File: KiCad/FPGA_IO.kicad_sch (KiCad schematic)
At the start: 18 parts, among them U502 XC7S50FTGB196

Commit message: replaced SAR-ADC with Sigma-Delta-Converter
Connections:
- net ADC.COMP: no longer names the net of U502.B6 (IO_0_34)
- net ADC.D0: no longer names the net of U502.D1 (IO_L11P_T1_SRCC_34)
- net ADC.D1: no longer names the net of U502.D2 (IO_L10N_T1_34)
- net ADC.D2: no longer names the net of U502.B1 (IO_L5N_T0_34)
- net ADC.D3 renamed ADC.FB_out0
- net ADC.D4: no longer names the net of U502.B2 (IO_L5P_T0_34)
- net ADC.D5 renamed ADC.SD_in0
- net ADC.D6: no longer names the net of U502.B3 (IO_L3P_T0_DQS_34)
- net ADC.D7 renamed ADC.SD_in1
- net ADC.SEL: no longer names the net of U502.B5 (IO_L4P_T0_34)
- net ADC.SH renamed ADC.FB_out1

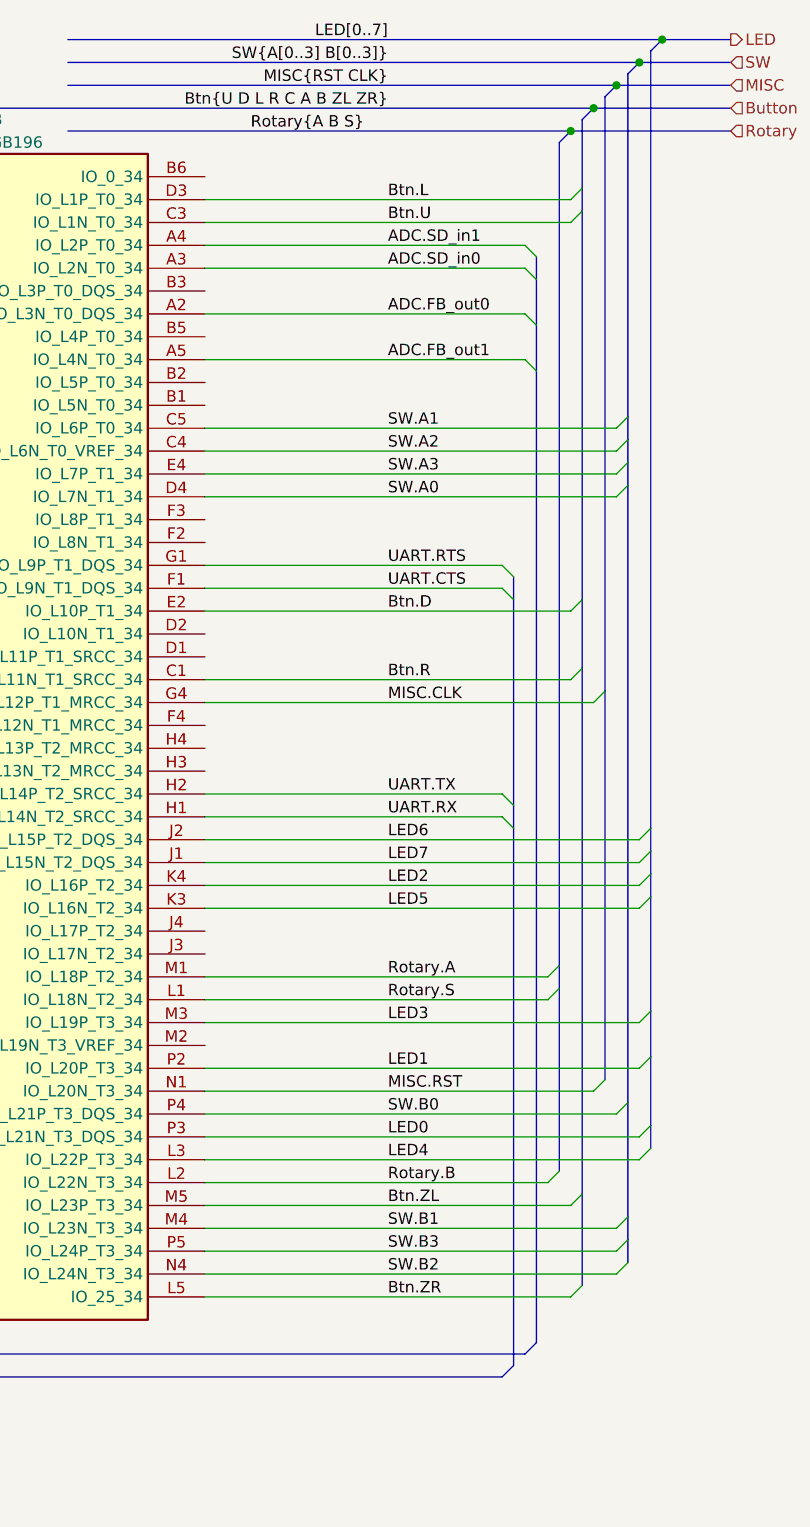
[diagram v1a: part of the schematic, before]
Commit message: Vorberitung für micro-SD
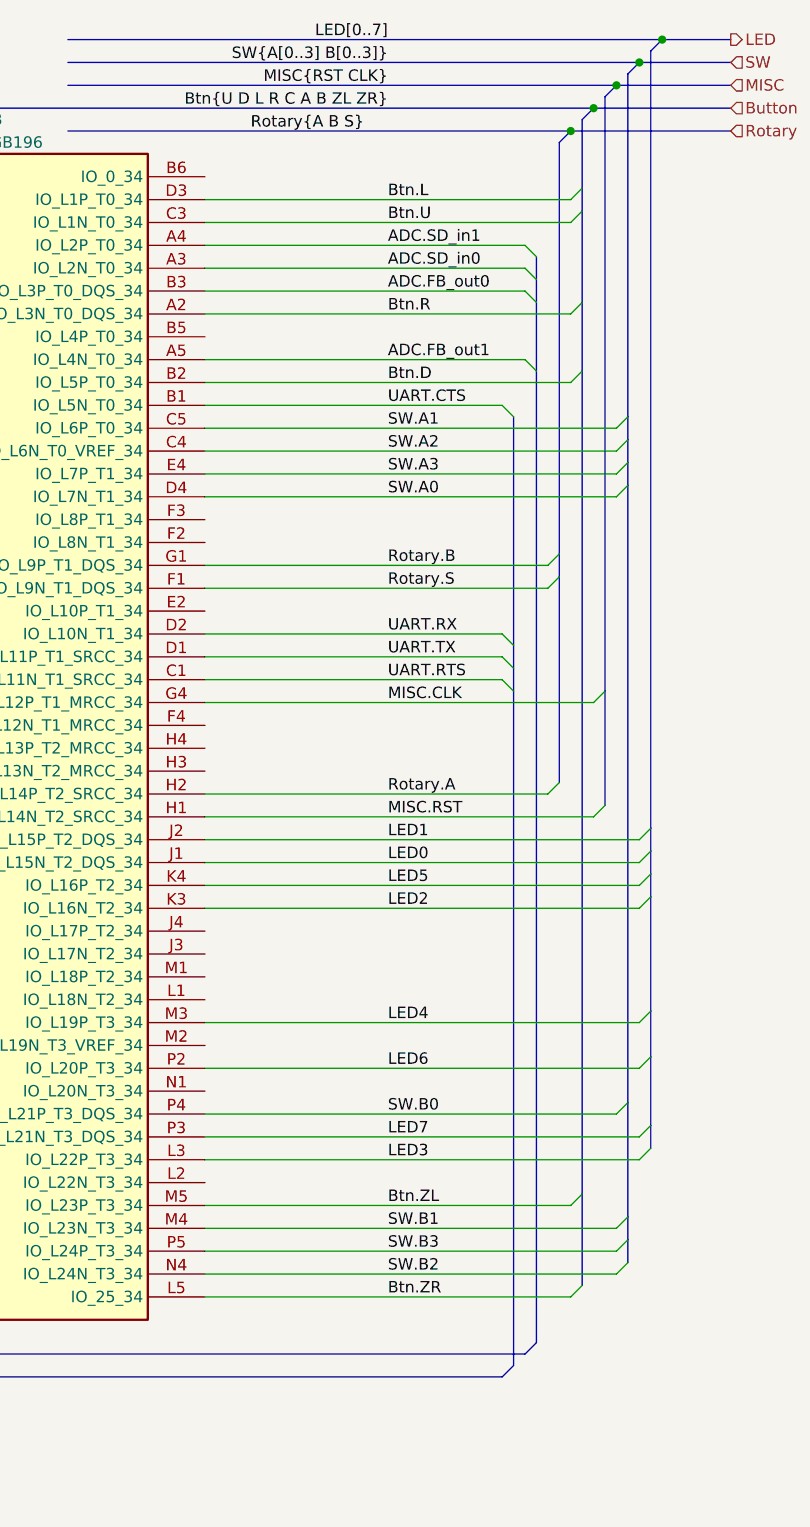
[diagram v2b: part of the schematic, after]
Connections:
- net ADC.FB_out0: now also U502.B3 (IO_L3P_T0_DQS_34); no longer U502.A2 (IO_L3N_T0_DQS_34)
- net Btn.D: now also U502.B2 (IO_L5P_T0_34); no longer U502.E2 (IO_L10P_T1_34)
- net Btn.R: now also U502.A2 (IO_L3N_T0_DQS_34); no longer U502.C1 (IO_L11N_T1_SRCC_34)
- net LED0: now also U502.J1 (IO_L15N_T2_DQS_34); no longer U502.P3 (IO_L21N_T3_DQS_34)
- net LED1: now also U502.J2 (IO_L15P_T2_DQS_34); no longer U502.P2 (IO_L20P_T3_34)
- net LED2: now also U502.K3 (IO_L16N_T2_34); no longer U502.K4 (IO_L16P_T2_34)
- net LED3: now also U502.L3 (IO_L22P_T3_34); no longer U502.M3 (IO_L19P_T3_34)
- net LED4: now also U502.M3 (IO_L19P_T3_34); no longer U502.L3 (IO_L22P_T3_34)
- net LED5: now also U502.K4 (IO_L16P_T2_34); no longer U502.K3 (IO_L16N_T2_34)
- net LED6: now also U502.P2 (IO_L20P_T3_34); no longer U502.J2 (IO_L15P_T2_DQS_34)
- net LED7: now also U502.P3 (IO_L21N_T3_DQS_34); no longer U502.J1 (IO_L15N_T2_DQS_34)
- net MISC.RST: now also U502.H1 (IO_L14N_T2_SRCC_34); no longer U502.N1 (IO_L20N_T3_34)
- net Rotary.A: now also U502.H2 (IO_L14P_T2_SRCC_34); no longer U502.M1 (IO_L18P_T2_34)
- net Rotary.B: now also U502.G1 (IO_L9P_T1_DQS_34); no longer U502.L2 (IO_L22N_T3_34)
- net Rotary.S: now also U502.F1 (IO_L9N_T1_DQS_34); no longer U502.L1 (IO_L18N_T2_34)
- net UART.CTS: now also U502.B1 (IO_L5N_T0_34); no longer U502.F1 (IO_L9N_T1_DQS_34)
- net UART.RTS: now also U502.C1 (IO_L11N_T1_SRCC_34); no longer U502.G1 (IO_L9P_T1_DQS_34)
- net UART.RX: now also U502.D2 (IO_L10N_T1_34); no longer U502.H1 (IO_L14N_T2_SRCC_34)
- net UART.TX: now also U502.D1 (IO_L11P_T1_SRCC_34); no longer U502.H2 (IO_L14P_T2_SRCC_34)

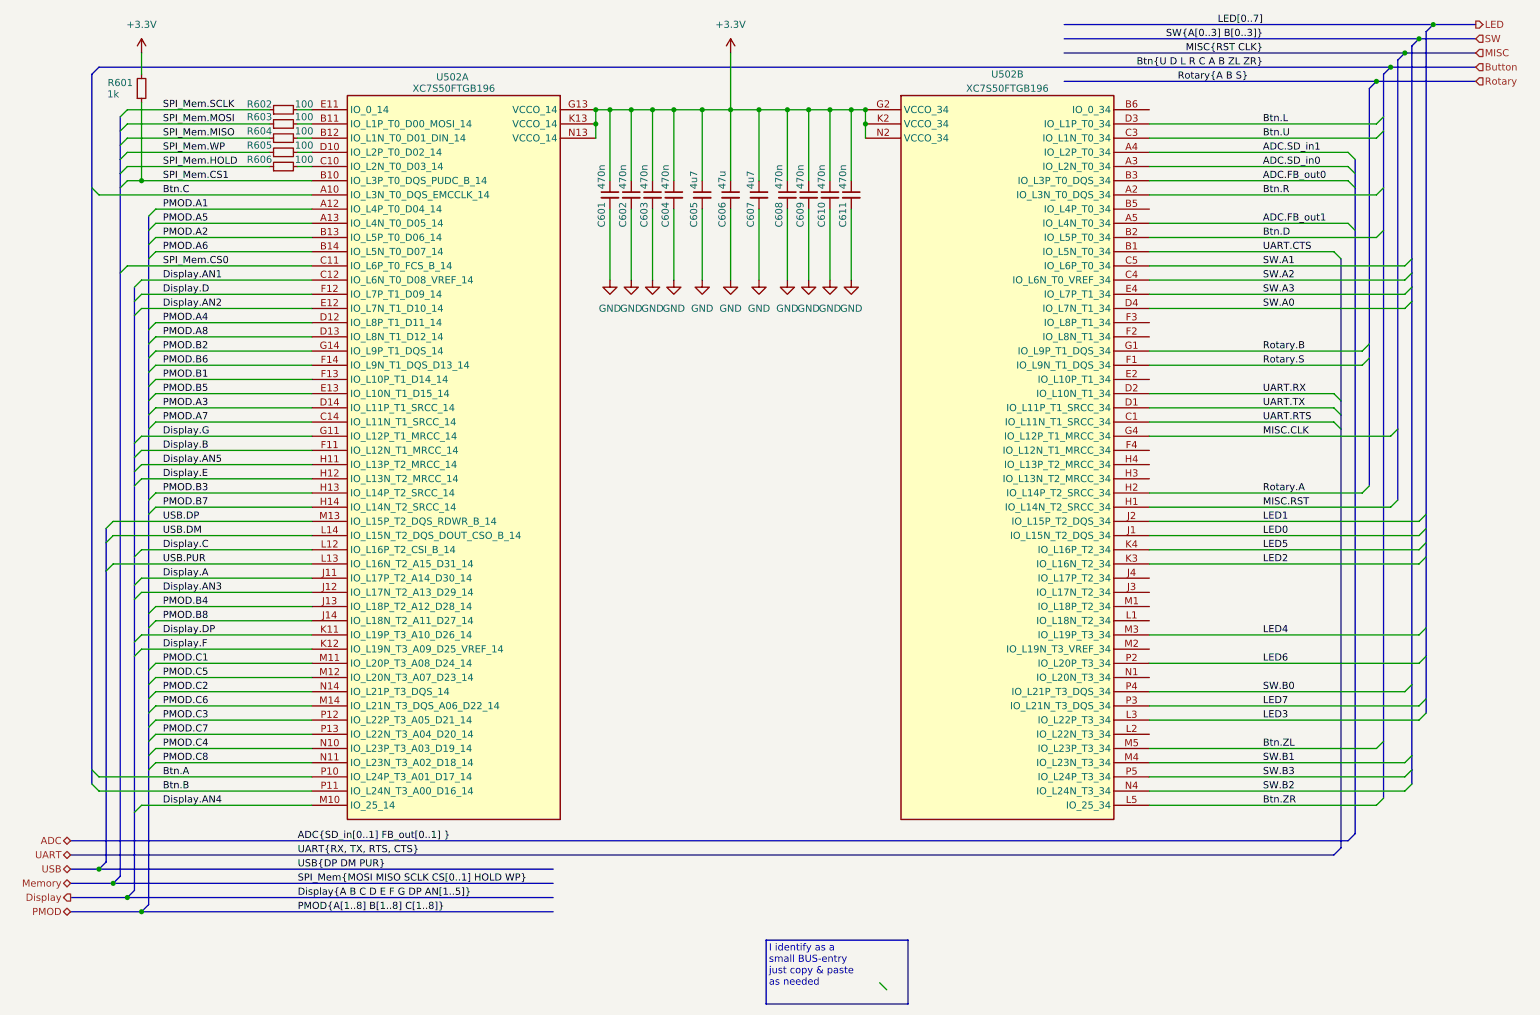
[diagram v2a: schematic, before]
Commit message: micro-SD hinzugefügt
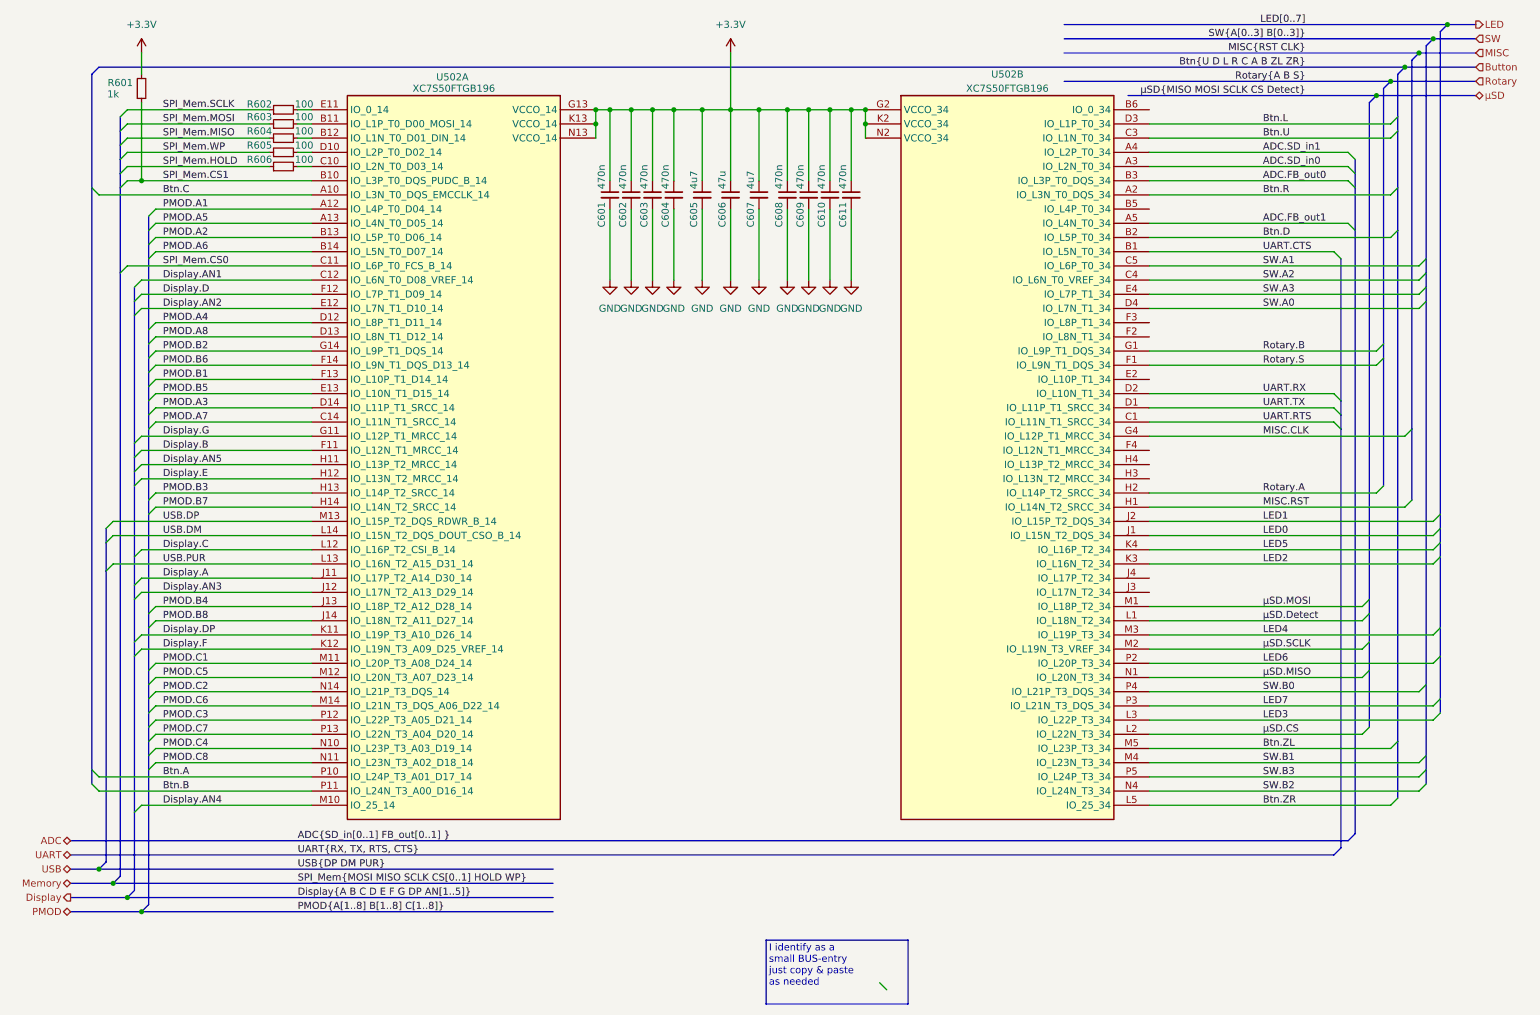
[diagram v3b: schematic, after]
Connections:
- net μSD.Detect: now reaches U502.L1 (IO_L18N_T2_34)
- net μSD.CS: now reaches U502.L2 (IO_L22N_T3_34)
- net μSD.MOSI: now reaches U502.M1 (IO_L18P_T2_34)
- net μSD.SCLK: now reaches U502.M2 (IO_L19N_T3_VREF_34)
- net μSD.MISO: now reaches U502.N1 (IO_L20N_T3_34)

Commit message: Pinout und Silkscreen angepasst
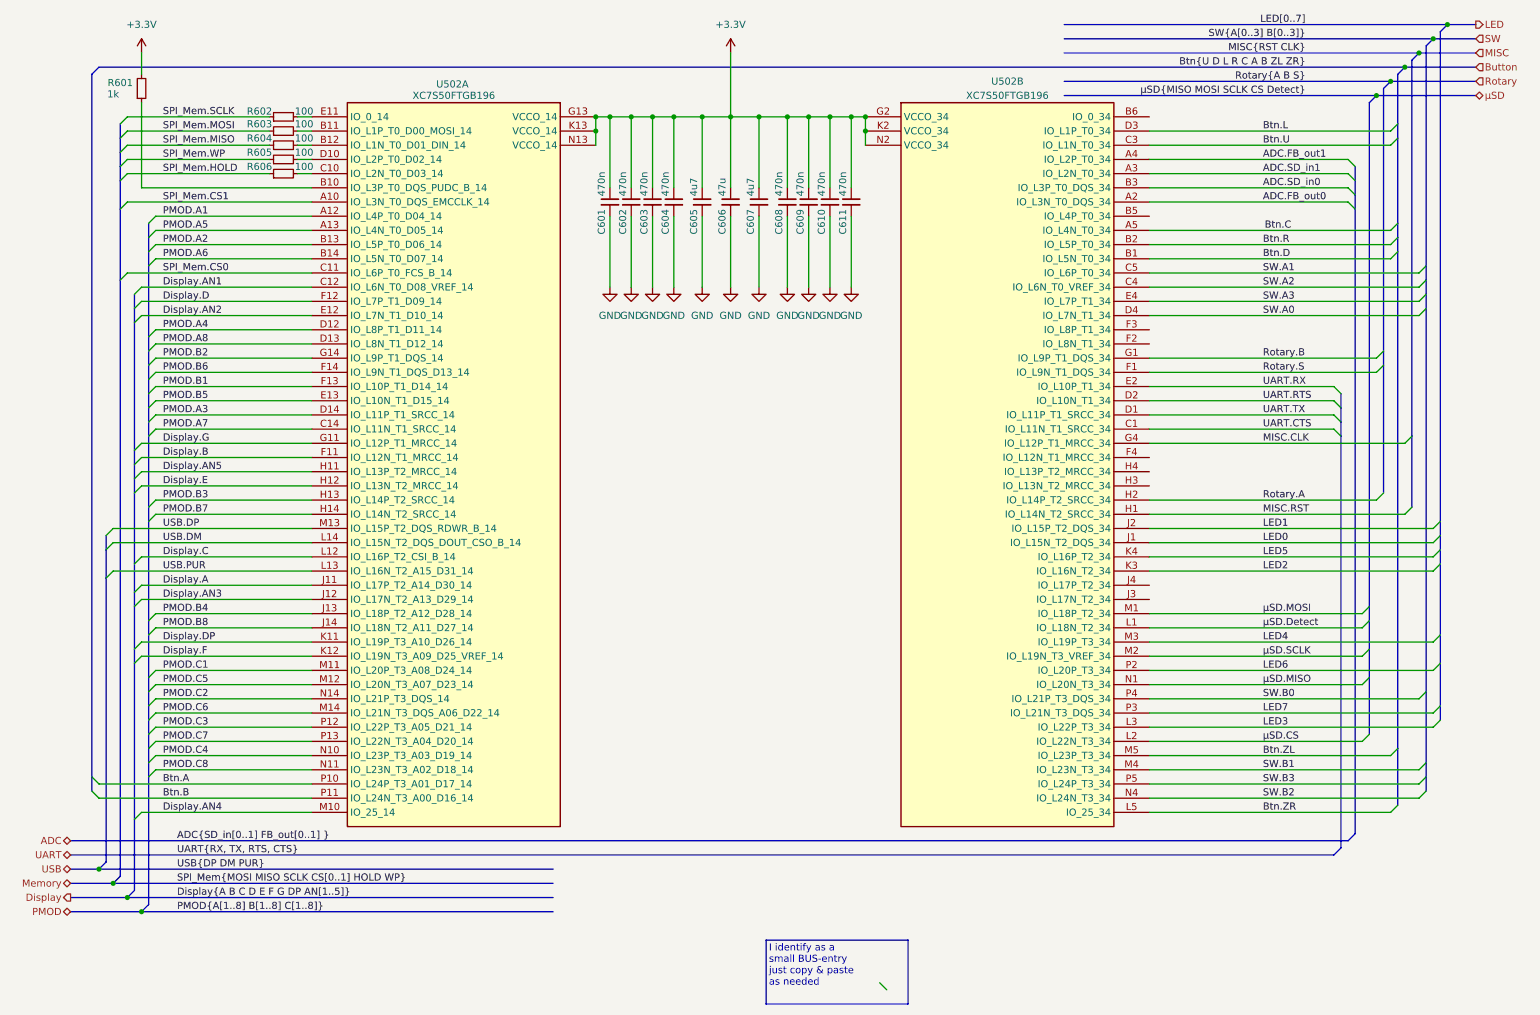
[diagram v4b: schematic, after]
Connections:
- net ADC.FB_out0: now also U502.A2 (IO_L3N_T0_DQS_34); no longer U502.B3 (IO_L3P_T0_DQS_34)
- net ADC.FB_out1: now also U502.A4 (IO_L2P_T0_34); no longer U502.A5 (IO_L4N_T0_34)
- net ADC.SD_in0: now also U502.B3 (IO_L3P_T0_DQS_34); no longer U502.A3 (IO_L2N_T0_34)
- net ADC.SD_in1: now also U502.A3 (IO_L2N_T0_34); no longer U502.A4 (IO_L2P_T0_34)
- net Btn.C: now also U502.A5 (IO_L4N_T0_34); no longer U502.A10 (IO_L3N_T0_DQS_EMCCLK_14)
- net Btn.D: now also U502.B1 (IO_L5N_T0_34); no longer U502.B2 (IO_L5P_T0_34)
- net Btn.R: now also U502.B2 (IO_L5P_T0_34); no longer U502.A2 (IO_L3N_T0_DQS_34)
- net SPI_Mem.CS1: now also U502.A10 (IO_L3N_T0_DQS_EMCCLK_14); no longer R601.1, U502.B10 (IO_L3P_T0_DQS_PUDC_B_14)
- net UART.CTS: now also U502.C1 (IO_L11N_T1_SRCC_34); no longer U502.B1 (IO_L5N_T0_34)
- net UART.RTS: now also U502.D2 (IO_L10N_T1_34); no longer U502.C1 (IO_L11N_T1_SRCC_34)
- net UART.RX: now also U502.E2 (IO_L10P_T1_34); no longer U502.D2 (IO_L10N_T1_34)
- new net: R601.1, U502.B10 (IO_L3P_T0_DQS_PUDC_B_14)
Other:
- moved on the sheet: C601, C602, C603, C604, C605, C606, C607, C608, C609, C610, C611, R602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

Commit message: LEDs zur Visualisierung des ausgewählten FPGAs
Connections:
- net μSD.CS: now also U502.L1 (IO_L18N_T2_34); no longer U502.L2 (IO_L22N_T3_34)
- net μSD.Detect: now also U502.N1 (IO_L20N_T3_34); no longer U502.L1 (IO_L18N_T2_34)
- net μSD.MISO: now also U502.M2 (IO_L19N_T3_VREF_34); no longer U502.N1 (IO_L20N_T3_34)
- net μSD.MOSI: now also U502.L2 (IO_L22N_T3_34); no longer U502.M1 (IO_L18P_T2_34)
- net μSD.SCLK: now also U502.M1 (IO_L18P_T2_34); no longer U502.M2 (IO_L19N_T3_VREF_34)
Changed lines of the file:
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@@
 	)
 	(label "μSD.CS"
-		(at 236.22 143.51 0)
+		(at 236.22 123.19 0)
 		(effects
 			(font
@@
 	)
 	(label "μSD.MISO"
-		(at 236.22 133.35 0)
+		(at 236.22 128.27 0)
 		(effects
 			(font
@@
 	)
 	(label "μSD.Detect"
-		(at 236.22 123.19 0)
+		(at 236.22 133.35 0)
 		(effects
 			(font
@@
 	)
 	(label "μSD.MOSI"
-		(at 236.22 120.65 0)
+		(at 236.22 143.51 0)
 		(effects
 			(font
@@
 	)
 	(label "μSD.SCLK"
-		(at 236.22 128.27 0)
-		(effects
-			(font
+		(at 236.22 120.65 0)
+		(effects
+			(font
